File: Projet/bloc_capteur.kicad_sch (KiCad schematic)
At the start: 12 parts, among them J401 optiqueGauche, J402 couleursDroit, J403 couleursGauche, J404 optiqueDroit, J405 tofGauche, J406 tofDroit

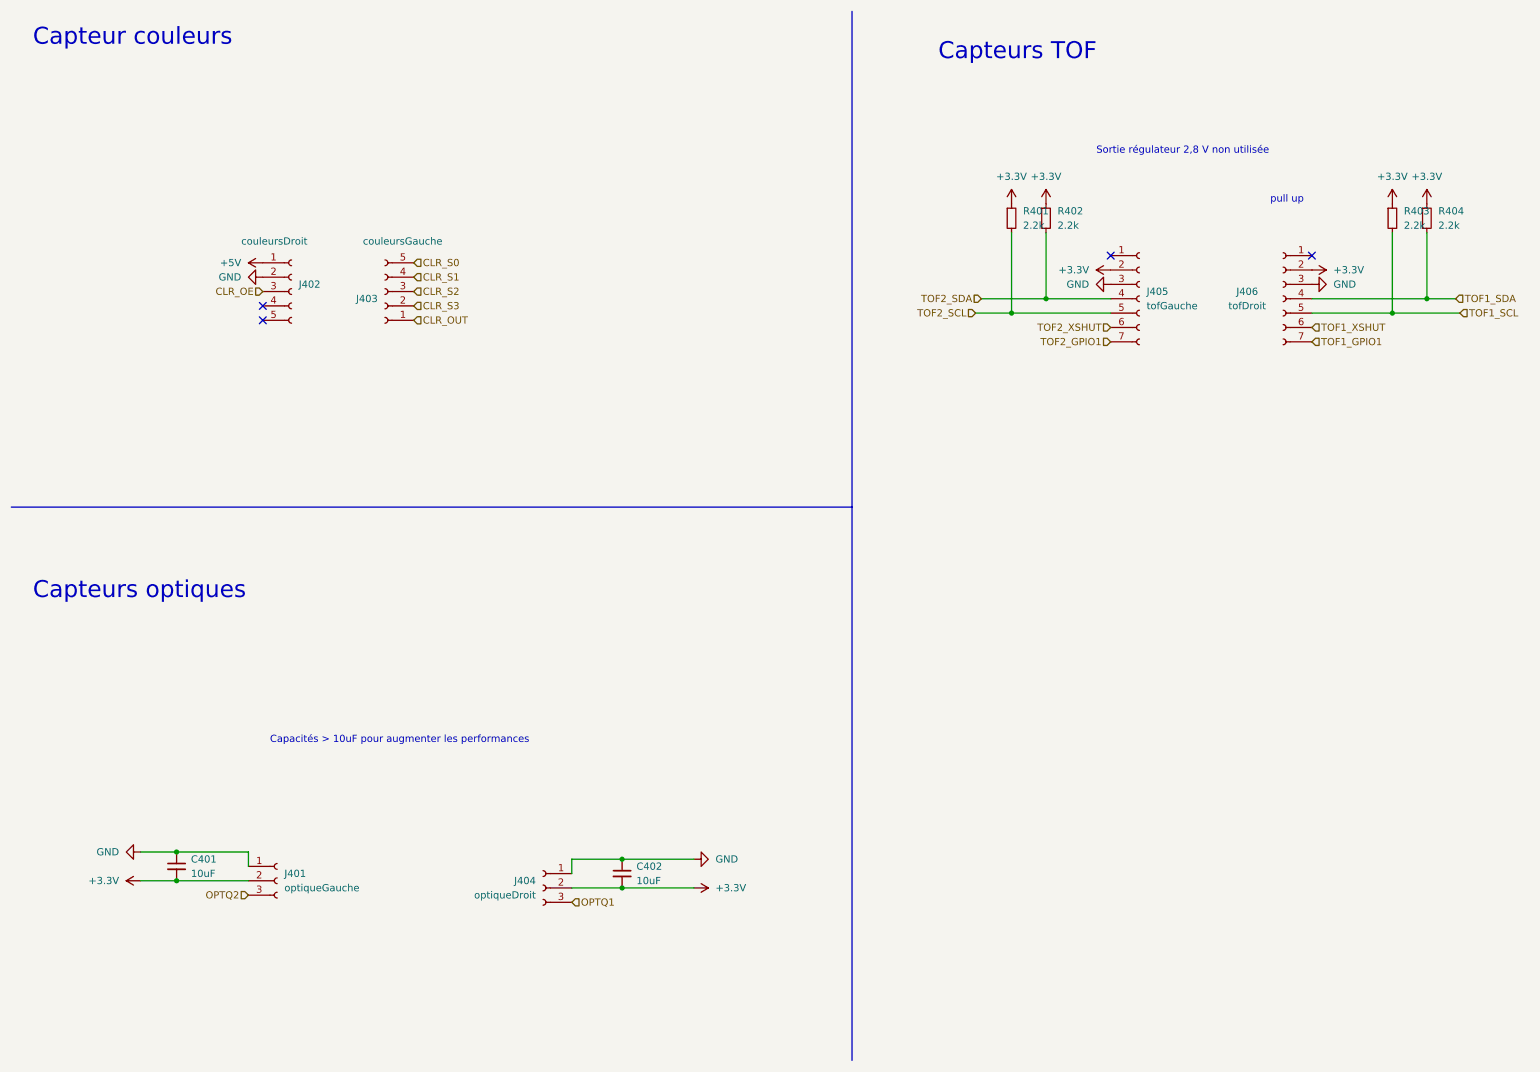
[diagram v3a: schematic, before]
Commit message: PCB_ROUTAGE_Modif
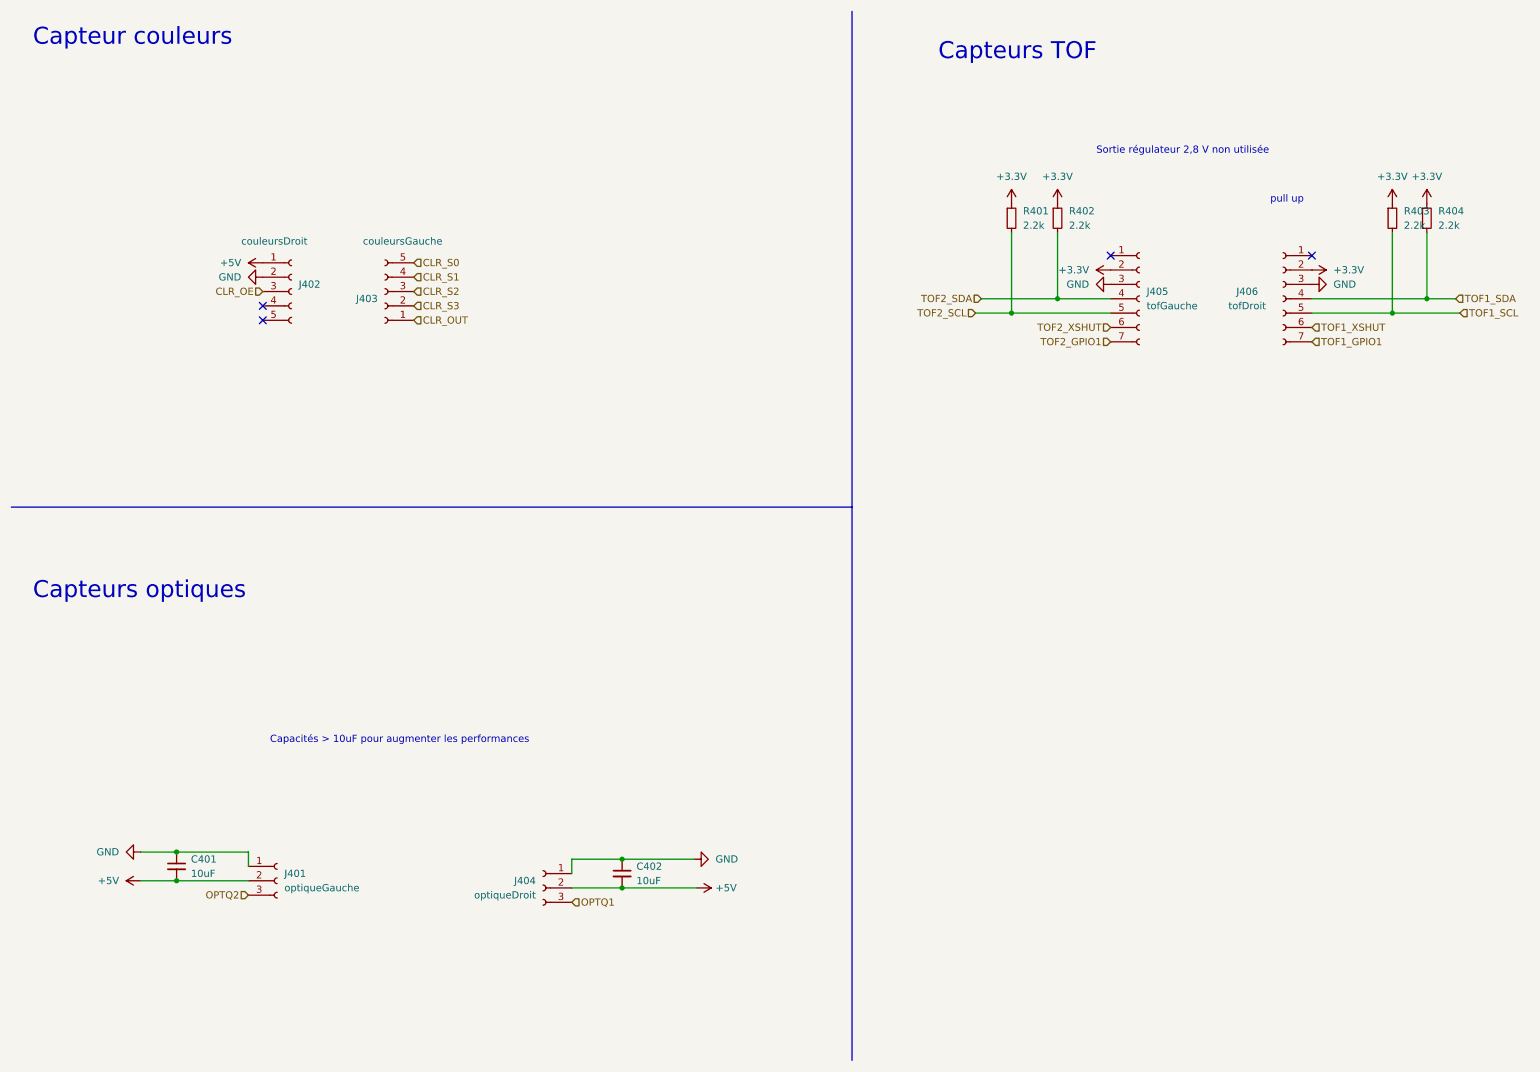
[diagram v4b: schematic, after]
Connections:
- net +3.3V: no longer C401.2, C402.2, J401.2 (Pin_2), J404.2 (Pin_2)
- net +5V: now also C401.2, C402.2, J401.2 (Pin_2), J404.2 (Pin_2)
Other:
- moved on the sheet: R402
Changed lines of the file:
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@@
 (kicad_sch (version 20211123) (generator eeschema)
   (paper "A4")
+  (junction (at 41.91 161.29) (diameter 0) (color 0 0 0 0)
+  )
+  (junction (at 262.89 63.5) (diameter 0) (color 0 0 0 0)
+  )
   (junction (at 41.91 166.37) (diameter 0) (color 0 0 0 0)
   )
-  (junction (at 41.91 161.29) (diameter 0) (color 0 0 0 0)
-  )
-  (junction (at 262.89 63.5) (diameter 0) (color 0 0 0 0)
-  )
   (junction (at 120.65 162.56) (diameter 0) (color 0 0 0 0)
   )
+  (junction (at 120.65 167.64) (diameter 0) (color 0 0 0 0)
+  )
   (junction (at 256.794 66.04) (diameter 0) (color 0 0 0 0)
   )
-  (junction (at 120.65 167.64) (diameter 0) (color 0 0 0 0)
-  )
   (junction (at 189.484 66.04) (diameter 0) (color 0 0 0 0)
   )
-  (junction (at 195.58 63.5) (diameter 0) (color 0 0 0 0)
+  (junction (at 197.612 63.5) (diameter 0) (color 0 0 0 0)
   )
   (no_connect (at 57.15 64.77))
@@
   (no_connect (at 242.57 55.88))
   (no_connect (at 57.15 67.31))
-  (wire (pts (xy 195.58 63.5) (xy 207.01 63.5))
+  (wire (pts (xy 197.612 63.5) (xy 207.01 63.5))
     (stroke (width 0) (type default) (color 0 0 0 0))
   )
@@
     (stroke (width 0) (type default) (color 0 0 0 0))
   )
-  (wire (pts (xy 184.15 63.5) (xy 195.58 63.5))
+  (wire (pts (xy 184.15 63.5) (xy 197.612 63.5))
     (stroke (width 0) (type default) (color 0 0 0 0))
   )
@@
     (stroke (width 0) (type default) (color 0 0 0 0))
   )
+  (wire (pts (xy 111.76 167.64) (xy 120.65 167.64))
+    (stroke (width 0) (type default) (color 0 0 0 0))
+  )
+  (wire (pts (xy 120.65 167.64) (xy 133.858 167.64))
+    (stroke (width 0) (type default) (color 0 0 0 0))
+  )
+  (wire (pts (xy 41.91 166.37) (xy 54.61 166.37))
+    (stroke (width 0) (type default) (color 0 0 0 0))
+  )
+  (wire (pts (xy 267.97 63.5) (xy 262.89 63.5))
+    (stroke (width 0) (type default) (color 0 0 0 0))
+  )
+  (wire (pts (xy 111.76 162.56) (xy 120.65 162.56))
+    (stroke (width 0) (type default) (color 0 0 0 0))
+  )
   (wire (pts (xy 35.56 166.37) (xy 41.91 166.37))
     (stroke (width 0) (type default) (color 0 0 0 0))
   )
-  (wire (pts (xy 111.76 167.64) (xy 120.65 167.64))
-    (stroke (width 0) (type default) (color 0 0 0 0))
-  )
-  (wire (pts (xy 41.91 166.37) (xy 54.61 166.37))
-    (stroke (width 0) (type default) (color 0 0 0 0))
-  )
-  (wire (pts (xy 267.97 63.5) (xy 262.89 63.5))
-    (stroke (width 0) (type default) (color 0 0 0 0))
-  )
-  (wire (pts (xy 120.65 167.64) (xy 133.35 167.64))
-    (stroke (width 0) (type default) (color 0 0 0 0))
-  )
-  (wire (pts (xy 111.76 162.56) (xy 120.65 162.56))
-    (stroke (width 0) (type default) (color 0 0 0 0))
-  )
   (wire (pts (xy 262.89 51.816) (xy 262.89 63.5))
     (stroke (width 0) (type default) (color 0 0 0 0))
@@
     (stroke (width 0) (type default) (color 0 0 0 0))
   )
-  (wire (pts (xy 195.58 51.816) (xy 195.58 63.5))
+  (wire (pts (xy 197.612 51.816) (xy 197.612 63.5))
     (stroke (width 0) (type default) (color 0 0 0 0))
   )
@@
     (pin "3")
   )
+  (symbol (lib_id "power:+5V") (at 35.56 166.37 90) (unit 1)
+    (in_bom yes) (on_board yes) (fields_autoplaced)
+    (property "Reference" "#PWR0112" (id 0) (at 39.37 166.37 0)
+      (effects (font (size 1.27 1.27)) hide)
+    )
+    (property "Value" "+5V" (id 1) (at 31.75 166.3699 90)
+      (effects (font (size 1.27 1.27)) (justify left))
+    )
+    (property "Footprint" "" (id 2) (at 35.56 166.37 0)
+      (effects (font (size 1.27 1.27)) hide)
+    )
+    (property "Datasheet" "" (id 3) (at 35.56 166.37 0)
+      (effects (font (size 1.27 1.27)) hide)
+    )
+    (pin "1")
+  )
   (symbol (lib_id "Connector:Conn_01x03_Female") (at 106.68 167.64 0) (mirror y) (unit 1)
     (in_bom yes) (on_board yes) (fields_autoplaced)
@@
     (pin "2")
     (pin "3")
+  )
+  (symbol (lib_id "power:+5V") (at 133.858 167.64 270) (unit 1)
+    (in_bom yes) (on_board yes) (fields_autoplaced)
+    (property "Reference" "#PWR0113" (id 0) (at 130.048 167.64 0)
+      (effects (font (size 1.27 1.27)) hide)
+    )
+    (property "Value" "+5V" (id 1) (at 137.16 167.6399 90)
+      (effects (font (size 1.27 1.27)) (justify left))
+    )
+    (property "Footprint" "" (id 2) (at 133.858 167.64 0)
+      (effects (font (size 1.27 1.27)) hide)
+    )
+    (property "Datasheet" "" (id 3) (at 133.858 167.64 0)
+      (effects (font (size 1.27 1.27)) hide)
+    )
+    (pin "1")
   )
   (symbol (lib_id "Connector:Conn_01x07_Female") (at 212.09 63.5 0) (unit 1)
@@
     (pin "5")
   )
-  (symbol (lib_id "power:+3.3V") (at 133.35 167.64 270) (mirror x) (unit 1)
-    (in_bom yes) (on_board yes) (fields_autoplaced)
-    (property "Reference" "#PWR0406" (id 0) (at 129.54 167.64 0)
-      (effects (font (size 1.27 1.27)) hide)
-    )
-    (property "Value" "+3.3V" (id 1) (at 137.16 167.6399 90)
-      (effects (font (size 1.27 1.27)) (justify left))
-    )
-    (property "Footprint" "" (id 2) (at 133.35 167.64 0)
-      (effects (font (size 1.27 1.27)) hide)
-    )
-    (property "Datasheet" "" (id 3) (at 133.35 167.64 0)
-      (effects (font (size 1.27 1.27)) hide)
-    )
-    (pin "1")
-  )
   (symbol (lib_id "power:GND") (at 242.57 60.96 90) (mirror x) (unit 1)
     (in_bom yes) (on_board yes) (fields_autoplaced)
@@
     (pin "1")
   )
-  (symbol (lib_id "power:+3.3V") (at 195.58 46.736 0) (unit 1)
-    (in_bom yes) (on_board yes) (fields_autoplaced)
-    (property "Reference" "#PWR0412" (id 0) (at 195.58 50.546 0)
-      (effects (font (size 1.27 1.27)) hide)
-    )
-    (property "Value" "+3.3V" (id 1) (at 195.58 41.91 0))
-    (property "Footprint" "" (id 2) (at 195.58 46.736 0)
-      (effects (font (size 1.27 1.27)) hide)
-    )
-    (property "Datasheet" "" (id 3) (at 195.58 46.736 0)
-      (effects (font (size 1.27 1.27)) hide)
-    )
-    (pin "1")
-  )
-  (symbol (lib_id "Device:R_Small") (at 195.58 49.276 0) (unit 1)
-    (in_bom yes) (on_board yes) (fields_autoplaced)
-    (property "Reference" "R402" (id 0) (at 197.612 48.0059 0)
-      (effects (font (size 1.27 1.27)) (justify left))
-    )
-    (property "Value" "2.2k" (id 1) (at 197.612 50.5459 0)
-      (effects (font (size 1.27 1.27)) (justify left))
-    )
-    (property "Footprint" "Resistor_SMD:R_0603_1608Metric_Pad0.98x0.95mm_HandSolder" (id 2) (at 195.58 49.276 0)
-      (effects (font (size 1.27 1.27)) hide)
-    )
-    (property "Datasheet" "~" (id 3) (at 195.58 49.276 0)
+  (symbol (lib_id "power:+3.3V") (at 197.612 46.736 0) (unit 1)
+    (in_bom yes) (on_board yes) (fields_autoplaced)
+    (property "Reference" "#PWR0412" (id 0) (at 197.612 50.546 0)
+      (effects (font (size 1.27 1.27)) hide)
+    )
+    (property "Value" "+3.3V" (id 1) (at 197.612 41.91 0))
+    (property "Footprint" "" (id 2) (at 197.612 46.736 0)
+      (effects (font (size 1.27 1.27)) hide)
+    )
+    (property "Datasheet" "" (id 3) (at 197.612 46.736 0)
+      (effects (font (size 1.27 1.27)) hide)
+    )
+    (pin "1")
+  )
+  (symbol (lib_id "Device:R_Small") (at 197.612 49.276 0) (unit 1)
+    (in_bom yes) (on_board yes) (fields_autoplaced)
+    (property "Reference" "R402" (id 0) (at 199.644 48.0059 0)
+      (effects (font (size 1.27 1.27)) (justify left))
+    )
+    (property "Value" "2.2k" (id 1) (at 199.644 50.5459 0)
+      (effects (font (size 1.27 1.27)) (justify left))
+    )
+    (property "Footprint" "Resistor_SMD:R_0603_1608Metric_Pad0.98x0.95mm_HandSolder" (id 2) (at 197.612 49.276 0)
+      (effects (font (size 1.27 1.27)) hide)
+    )
+    (property "Datasheet" "~" (id 3) (at 197.612 49.276 0)
       (effects (font (size 1.27 1.27)) hide)
     )
@@
       (effects (font (size 1.27 1.27)) hide)
     )
-    (pin "1")
-  )
-  (symbol (lib_id "power:+3.3V") (at 35.56 166.37 90) (unit 1)
-    (in_bom yes) (on_board yes) (fields_autoplaced)
-    (property "Reference" "#PWR0402" (id 0) (at 39.37 166.37 0)
-      (effects (font (size 1.27 1.27)) hide)
-    )
-    (property "Value" "+3.3V" (id 1) (at 31.75 166.3699 90)
-      (effects (font (size 1.27 1.27)) (justify left))
-    )
-    (property "Footprint" "" (id 2) (at 35.56 166.37 0)
-      (effects (font (size 1.27 1.27)) hide)
-    )
-    (property "Datasheet" "" (id 3) (at 35.56 166.37 0)
-      (effects (font (size 1.27 1.27)) hide)
-    )

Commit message: Routage_fini
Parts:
- J402: value couleursDroit -> couleursGauche
- J403: value couleursGauche -> couleursDroit
- J405: value tofGauche -> tofDroit
- J406: value tofDroit -> tofGauche
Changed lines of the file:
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@@
       (effects (font (size 1.27 1.27)) (justify left))
     )
-    (property "Value" "tofGauche" (id 1) (at 213.36 64.7699 0)
+    (property "Value" "tofDroit" (id 1) (at 213.36 64.7699 0)
       (effects (font (size 1.27 1.27)) (justify left))
     )
@@
       (effects (font (size 1.27 1.27)) (justify left))
     )
-    (property "Value" "couleursDroit" (id 1) (at 53.34 53.34 0)
+    (property "Value" "couleursGauche" (id 1) (at 53.34 53.34 0)
       (effects (font (size 1.27 1.27)) (justify left))
     )
@@
       (effects (font (size 1.27 1.27)) (justify left))
     )
-    (property "Value" "couleursGauche" (id 1) (at 88.9 53.34 0)
+    (property "Value" "couleursDroit" (id 1) (at 88.9 53.34 0)
       (effects (font (size 1.27 1.27)) (justify left))
     )
@@
     (in_bom yes) (on_board yes)
     (property "Reference" "J406" (id 0) (at 231.14 62.23 0))
-    (property "Value" "tofDroit" (id 1) (at 231.14 64.77 0))
+    (property "Value" "tofGauche" (id 1) (at 231.14 64.77 0))
     (property "Footprint" "Connector_JST:JST_XH_B7B-XH-A_1x07_P2.50mm_Vertical" (id 2) (at 237.49 63.5 0)
       (effects (font (size 1.27 1.27)) hide)

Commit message: Routage_Final
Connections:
- net GND: now also J402.5 (Pin_5)
- net CLR_LED: now reaches J402.4 (Pin_4)
- no-connect marks 4 -> 2
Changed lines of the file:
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@@
   (junction (at 197.612 63.5) (diameter 0) (color 0 0 0 0)
   )
-  (no_connect (at 57.15 64.77))
   (no_connect (at 207.01 55.88))
   (no_connect (at 242.57 55.88))
-  (no_connect (at 57.15 67.31))
   (wire (pts (xy 197.612 63.5) (xy 207.01 63.5))
     (stroke (width 0) (type default) (color 0 0 0 0))
@@
   )
   (wire (pts (xy 267.97 63.5) (xy 262.89 63.5))
+    (stroke (width 0) (type default) (color 0 0 0 0))
+  )
+  (wire (pts (xy 55.372 67.31) (xy 57.15 67.31))
     (stroke (width 0) (type default) (color 0 0 0 0))
   )
@@
   (hierarchical_label "CLR_S2" (shape input) (at 83.82 62.23 0)
     (effects (font (size 1.27 1.27)) (justify left))
+  )
+  (hierarchical_label "CLR_LED" (shape input) (at 57.15 64.77 180)
+    (effects (font (size 1.27 1.27)) (justify right))
   )
   (hierarchical_label "CLR_S3" (shape input) (at 83.82 64.77 0)
@@
     (pin "5")
   )
+  (symbol (lib_id "power:GND") (at 55.372 67.31 0) (unit 1)
+    (in_bom yes) (on_board yes) (fields_autoplaced)
+    (property "Reference" "#PWR?" (id 0) (at 55.372 73.66 0)
+      (effects (font (size 1.27 1.27)) hide)
+    )
+    (property "Value" "GND" (id 1) (at 55.372 72.39 0))
+    (property "Footprint" "" (id 2) (at 55.372 67.31 0)
+      (effects (font (size 1.27 1.27)) hide)
+    )
+    (property "Datasheet" "" (id 3) (at 55.372 67.31 0)
+      (effects (font (size 1.27 1.27)) hide)
+    )
+    (pin "1")
+  )
   (symbol (lib_id "power:GND") (at 242.57 60.96 90) (mirror x) (unit 1)
